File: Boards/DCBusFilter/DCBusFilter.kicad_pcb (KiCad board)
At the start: 4 copper layers, 89 x 75 mm, 11 parts, among them J1 TBP01R2-508-04BE

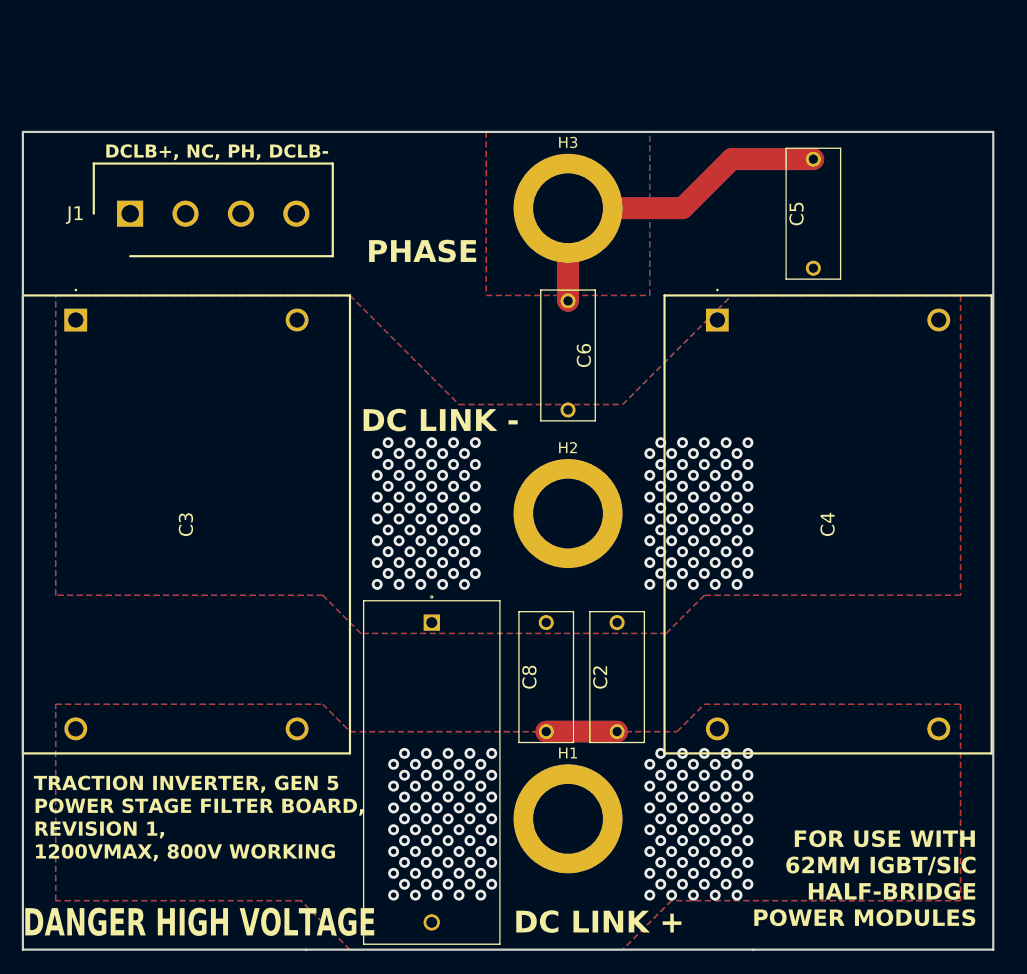
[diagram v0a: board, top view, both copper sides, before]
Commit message: add new caps board
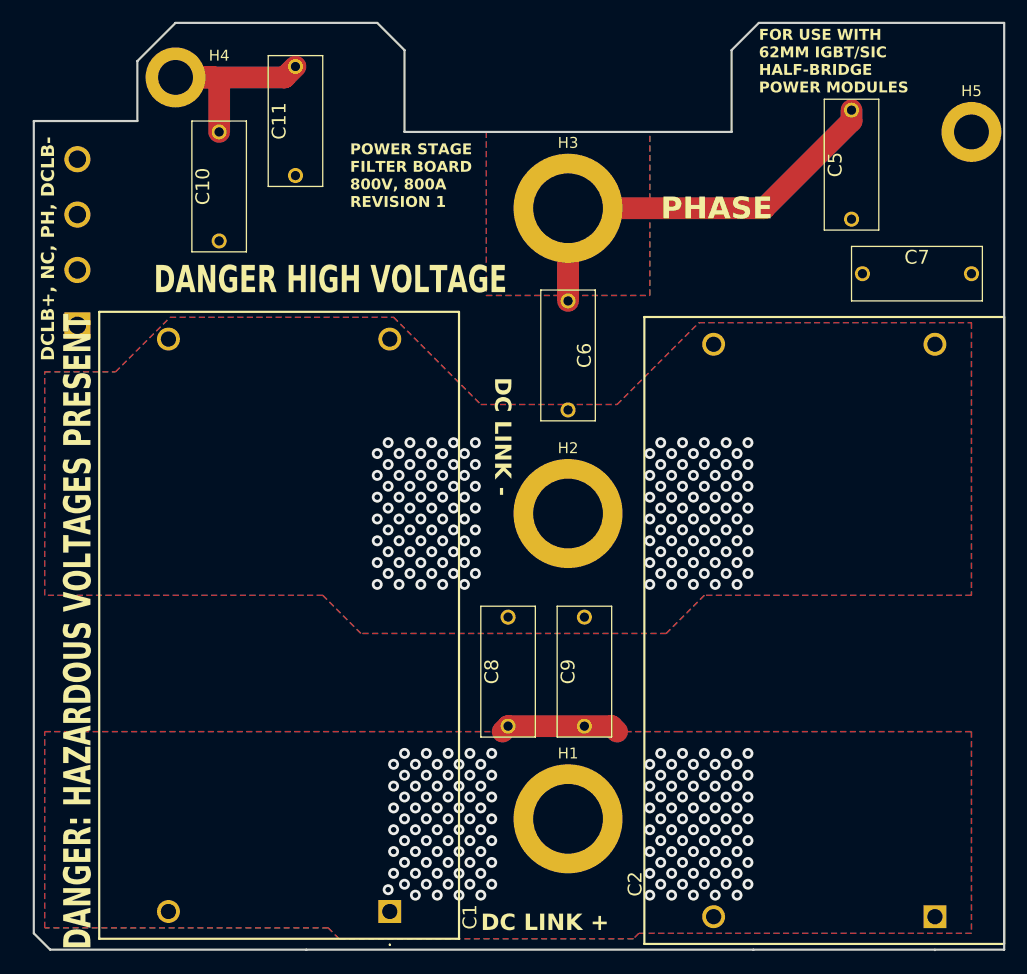
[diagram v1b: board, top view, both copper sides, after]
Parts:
- removed C3, C4: C4AQNBW5200M3LJ, InverterCom:C4AQNBW5200M3LJ
- added C10: VY1222M47Y5UQ6TV0, InverterCom:VY1222M47Y5UQ6TV0, F.Cu at (18.0, 0.00)
- added C11: VY1222M47Y5UQ6TV0, InverterCom:VY1222M47Y5UQ6TV0, F.Cu at (25.0, -6.00)
- added C7: VY1222M47Y5UQ6TV0, InverterCom:VY1222M47Y5UQ6TV0, F.Cu at (87.0, 13.0)
- added C9: VY1222M47Y5UQ6TV0, InverterCom:VY1222M47Y5UQ6TV0, F.Cu at (51.5, 44.5)
- added H4: MountingHole_Pad, MountingHole:MountingHole_3.2mm_M3_ISO14580_Pad, F.Cu at (14.0, -5.00)
- added H5: MountingHole_Pad, MountingHole:MountingHole_3.2mm_M3_ISO14580_Pad, F.Cu at (87.0, 0.00)
- C1: value B32774X0205K000 -> MKP1848S61010JY5B; footprint InverterCom:B32774X__31.5_x_12.5_ -> InverterCom:MKP1848S61010JY5B
- C2: value VY1222M47Y5UQ6TV0 -> MKP1848S61010JY5B; footprint InverterCom:VY1222M47Y5UQ6TV0 -> InverterCom:MKP1848S61010JY5B
- J1: moved to B.Cu
- moved C2 39.7 mm to (83.7, 72.0), turned to 90 degrees
- moved C1 26.8 mm to (33.6, 71.5), turned to 90 degrees
- moved J1 11.3 mm to (5.00, 17.7), turned to 90 degrees
- moved C5 5.70 mm to (76.0, -2.00)
- moved C8 3.54 mm to (44.5, 44.5)
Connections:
- C1 pad 1: /DC_LINK_- -> /DC_LINK_+
- C1 pad 2: /DC_LINK_+ -> /DC_LINK_-
- C2 pad 1: /DC_LINK_- -> /DC_LINK_+
- C2 pad 2: /DC_LINK_+ -> /DC_LINK_-
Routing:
- net /PHASE_LEG: track 71.6 -> 114.5 mm
- net /DC_LINK_+: track 101.8 -> 126.2 mm
- net /DC_LINK_-: track 9.78 -> 33.0 mm
- net /CHASSIS_GND: track 0.00 -> 20.1 mm
- net /CHASSIS_GND_1: track 0.00 -> 13.0 mm
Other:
- board size 89 x 75 mm -> 89 x 85 mm
- board text added: "DANGER: HAZARDOUS VOLTAGES PRESENT"
- board text added: "POWER STAGE FILTER BOARD 800V, 800A REVISION 1"
- board text added: "TRACTION INVERTER, GEN 5 POWER STAGE FILTER BOARD, REVISION 1, 800V, 800A"
- board text removed: "TRACTION INVERTER, GEN 5 POWER STAGE FILTER BOARD, REVISION 1, 1200VMAX, 800V WORKING"
